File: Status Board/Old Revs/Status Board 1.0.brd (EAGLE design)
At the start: 172.7 x 55.9 mm, 47 parts

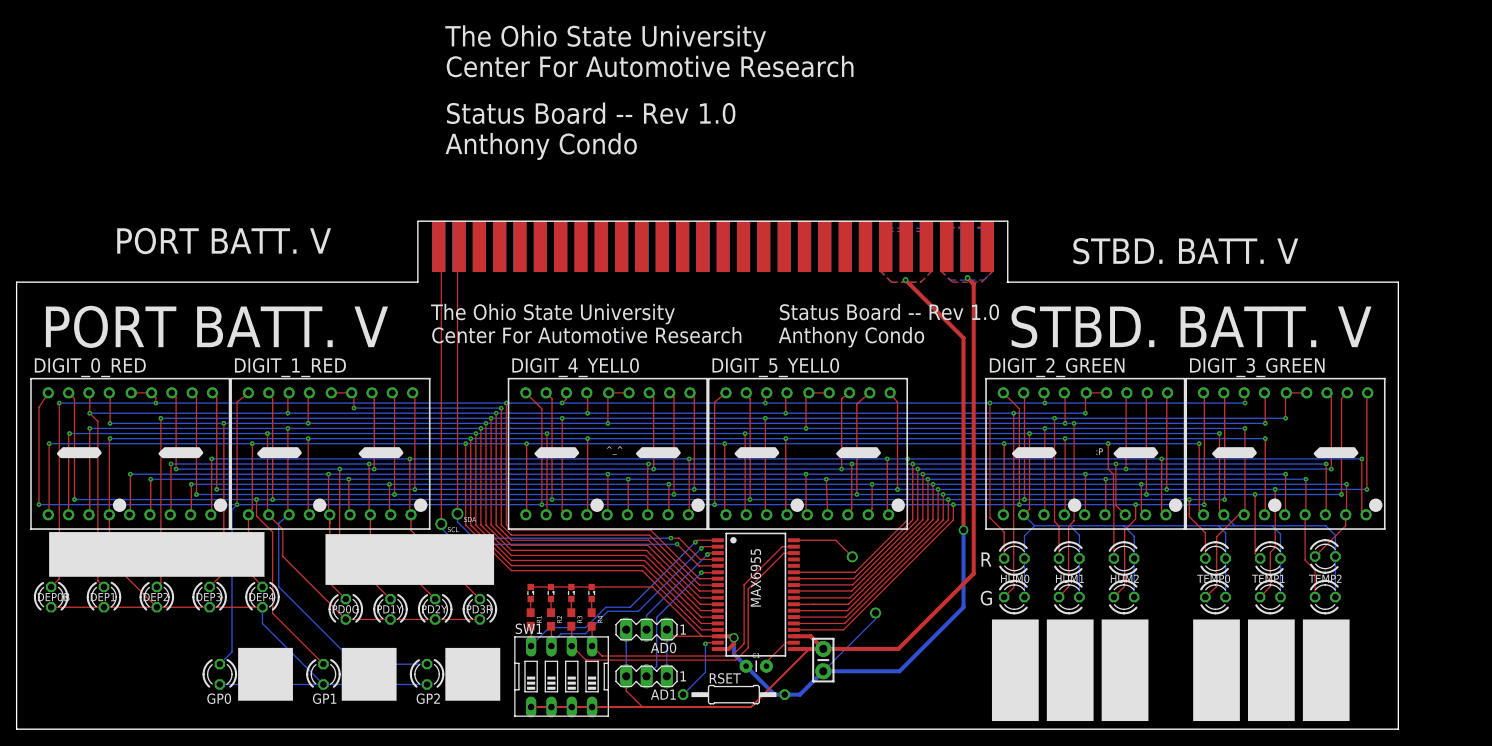
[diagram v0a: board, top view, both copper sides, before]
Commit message: Updated lables position and content
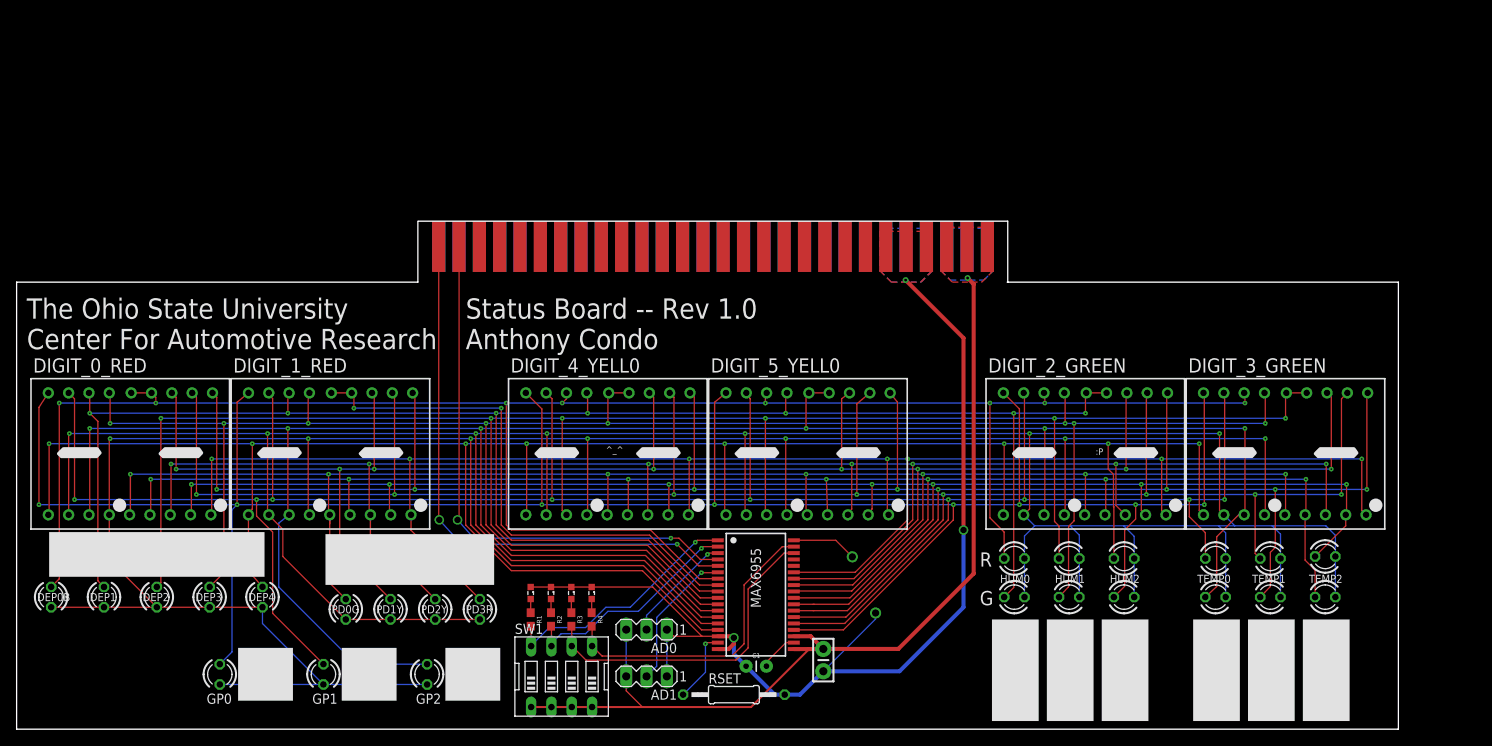
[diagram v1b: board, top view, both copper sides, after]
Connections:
- net 013 renamed N$40
- net AD0 renamed N$11
- net AD1 renamed N$12
- net ISET renamed N$46
- net O0 renamed N$20
- net O1 renamed N$21
- net O10 renamed N$30
- net O11 renamed N$31
- net O12 renamed N$32
- net O14 renamed N$34
- net O15 renamed N$35
- net O16 renamed N$36
- net O17 renamed N$37
- net O18 renamed N$38
- net O2 renamed N$22
- net O3 renamed N$23
- net O4 renamed N$26
- net O5 renamed N$27
- net O6 renamed N$33
- net O7 renamed N$56
- net O8 renamed N$15
- net O9 renamed N$29
- net OSC renamed N$13
- net P0 renamed N$4
- net P1 renamed N$5
- net P2 renamed N$6
- net P3 renamed N$7
- net P4 renamed N$8
- net SCL renamed N$2
- net SDA renamed N$43
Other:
- board text removed: "PORT BATT. V"
- board text removed: "SCL"
- board text removed: "SDA"
- board text removed: "STBD. BATT. V"
